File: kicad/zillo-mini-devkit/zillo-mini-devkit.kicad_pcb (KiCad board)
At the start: 2 copper layers, 29 x 49.3 mm, 9 parts, among them J1 Conn_01x19, J2 Conn_01x19, J3 Conn_01x08

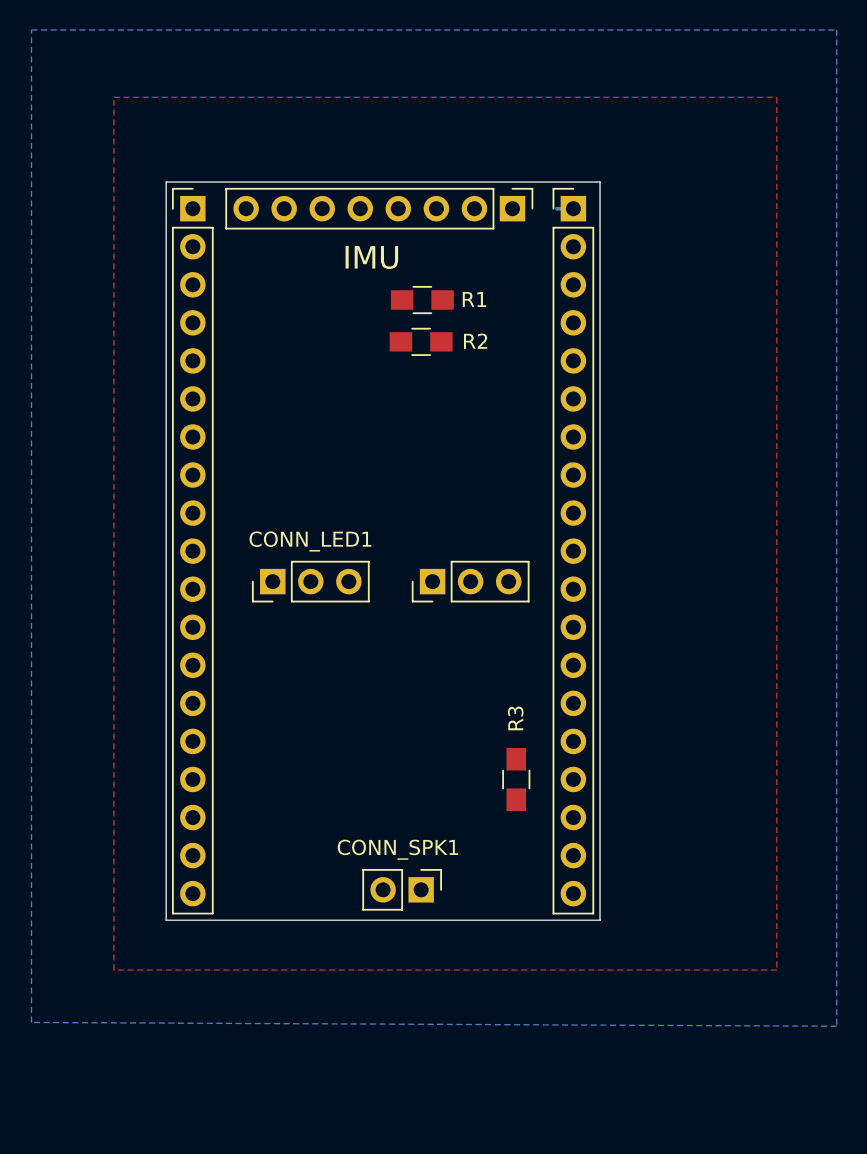
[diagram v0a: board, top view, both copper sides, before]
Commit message: update pcb&schematic: i2c ok
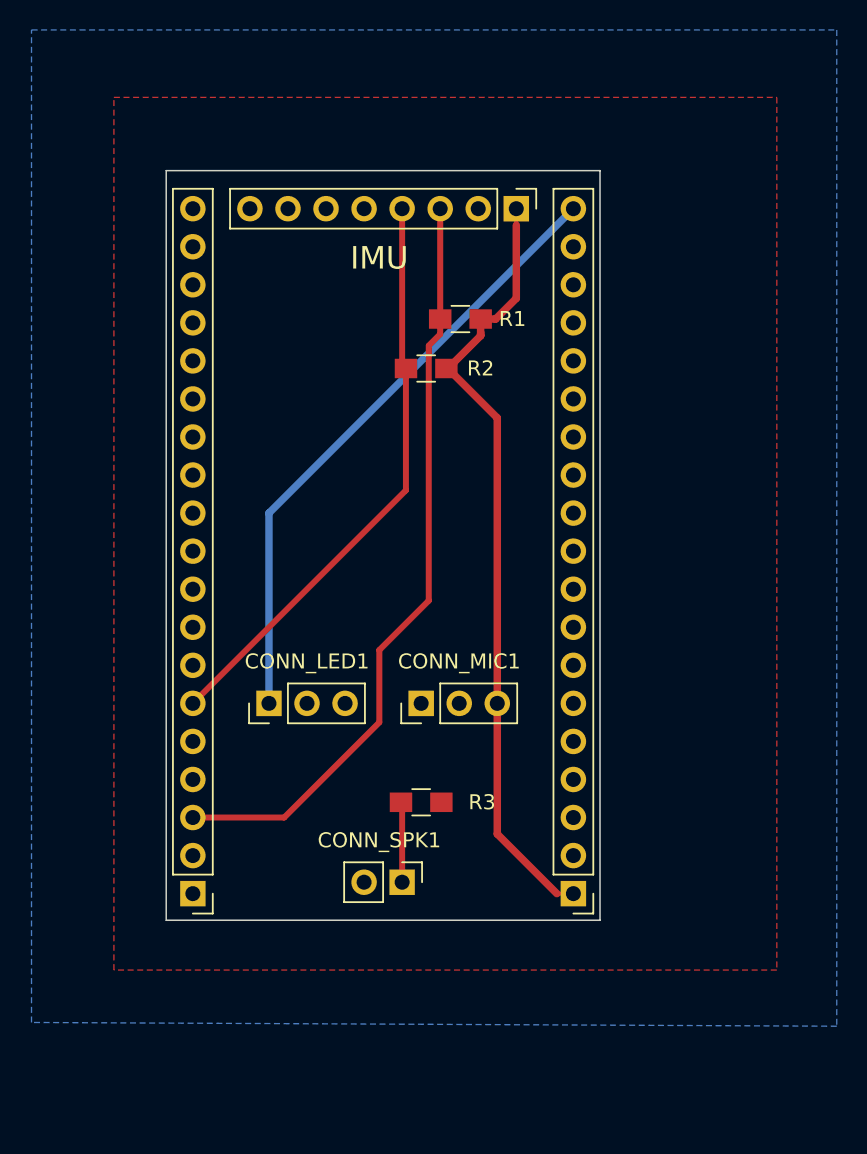
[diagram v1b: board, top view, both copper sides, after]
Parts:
- moved J1 45.7 mm to (33.0, 88.9), turned to 180 degrees
- moved J2 45.7 mm to (58.4, 88.9), turned to 180 degrees
- moved CONN_MIC1 8.16 mm to (48.3, 76.2)
- moved CONN_LED1 8.13 mm to (38.1, 76.2)
- moved R3 6.53 mm to (48.3, 82.8), turned to 180 degrees
- moved R1 2.84 mm to (50.9, 50.5)
- moved R2 1.81 mm to (48.6, 53.8)
- moved CONN_SPK1 1.37 mm to (47.0, 88.1)
- moved J3 0.25 mm to (54.6, 43.2)
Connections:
- CONN_LED1 pad 1: (no net) -> 5V
- CONN_LED1 pad 2: 5V -> (no net)
- J1 pad 1: (no net) -> GND
- J1 pad 19: GND -> (no net)
- J1 pad 3: (no net) -> SCL
- J1 pad 6: (no net) -> SDA
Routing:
- net 3V3: track 1.10 -> 52.6 mm
- net SCL: track 0.00 -> 51.0 mm
- net 5V: track 0.00 -> 41.4 mm
- net SDA: track 0.00 -> 39.0 mm
- net Net-(CONN_SPK1-Pad1): track 0.00 -> 5.37 mm
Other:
- board size 29 x 49.3 mm -> 29 x 50 mm

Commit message: kicad
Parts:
- added REF**: LOGO_RAT, zillo-mini-devkit:LOGO_RAT, F.Cu at (45.7, 63.8)
- added REF**: LOGO_PANDA, zillo-mini-devkit:LOGO_PANDA, F.Cu at (45.5, 49.0)
- R1, R2, R3: moved to B.Cu
- moved J3 32.6 mm to (37.8, 71.1), turned to 0 degrees
- moved R1 27.1 mm to (42.2, 76.2)
- moved R2 25.7 mm to (42.2, 78.7)
- moved CONN_LED1 20.9 mm to (33.0, 96.5)
- moved CONN_MIC1 20.9 mm to (53.3, 96.5)
- moved CONN_SPK1 9.21 mm to (43.2, 96.5), turned to 90 degrees
- moved R3 8.07 mm to (44.5, 89.9), turned to 270 degrees
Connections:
- CONN_LED1 pad 2: (no net) -> LEDMATRIX
- CONN_MIC1 pad 1: (no net) -> MICROPHONE
- J1 pad 7: (no net) -> GND
- J2 pad 11: (no net) -> LEDMATRIX
- J2 pad 14: (no net) -> GND
- J2 pad 5: (no net) -> MICROPHONE
- J2 pad 9: (no net) -> SPEAKER
- R3 pad 1: (no net) -> SPEAKER
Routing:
- net LEDMATRIX: track 0.00 -> 42.7 mm
- net SCL: track 51.0 -> 12.6 mm
- net SDA: track 39.0 -> 8.85 mm
- net SPEAKER: track 0.00 -> 25.7 mm, vias 0 -> 1
- net 5V: track 41.4 -> 65.1 mm
- net MICROPHONE: track 0.00 -> 20.3 mm
- net 3V3: track 52.6 -> 39.3 mm
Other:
- board size 29 x 50 mm -> 30.5 x 58.4 mm
- board text added: "&"
- board text added: "2019"
- board text added: "DrZoid"
- board text added: "Zilliq"
- board text added: "zillo-devkit-v1"
